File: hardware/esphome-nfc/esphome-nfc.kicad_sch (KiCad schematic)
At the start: 34 parts, among them U1 ESP32-C3-WROOM-02, U2 PN7160A1HN/C100Y, U3 AP2112K-3.3TRG1, U4 USBLC6-2P6, Y1 Crystal_GND24

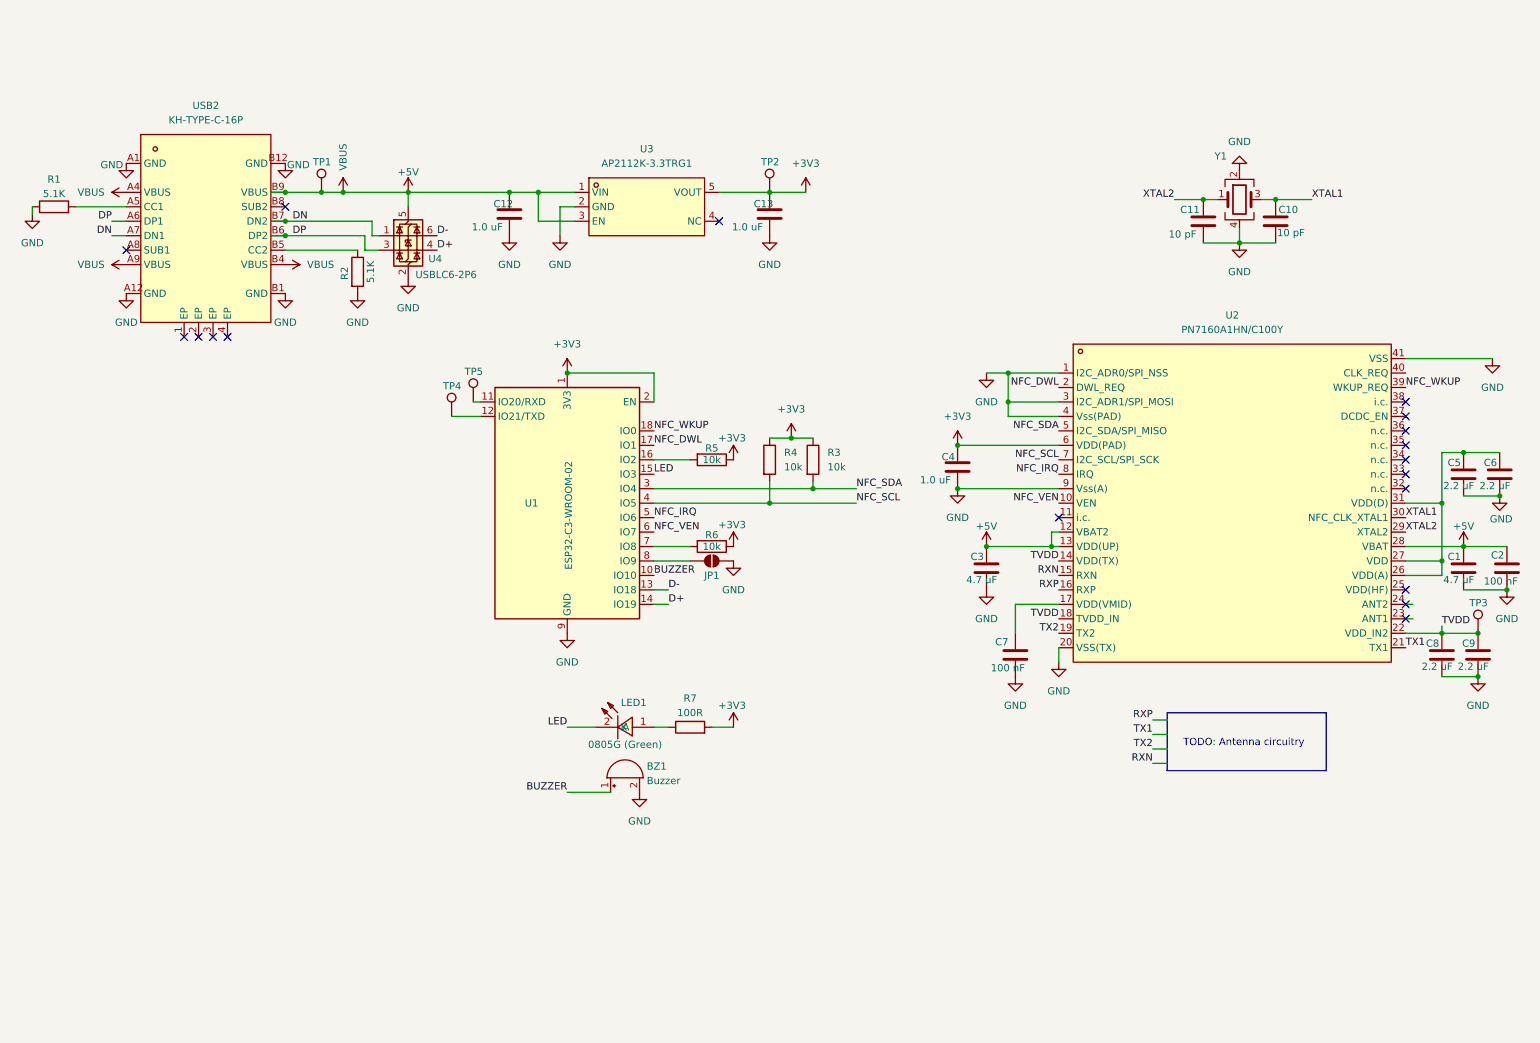
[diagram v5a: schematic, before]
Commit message: esphome-nfc final touches
* Add an antenna and corresponding matching circuitry
* Add a button (you never know...)
* Mark components I plan to solder manually as "Do Not Place"
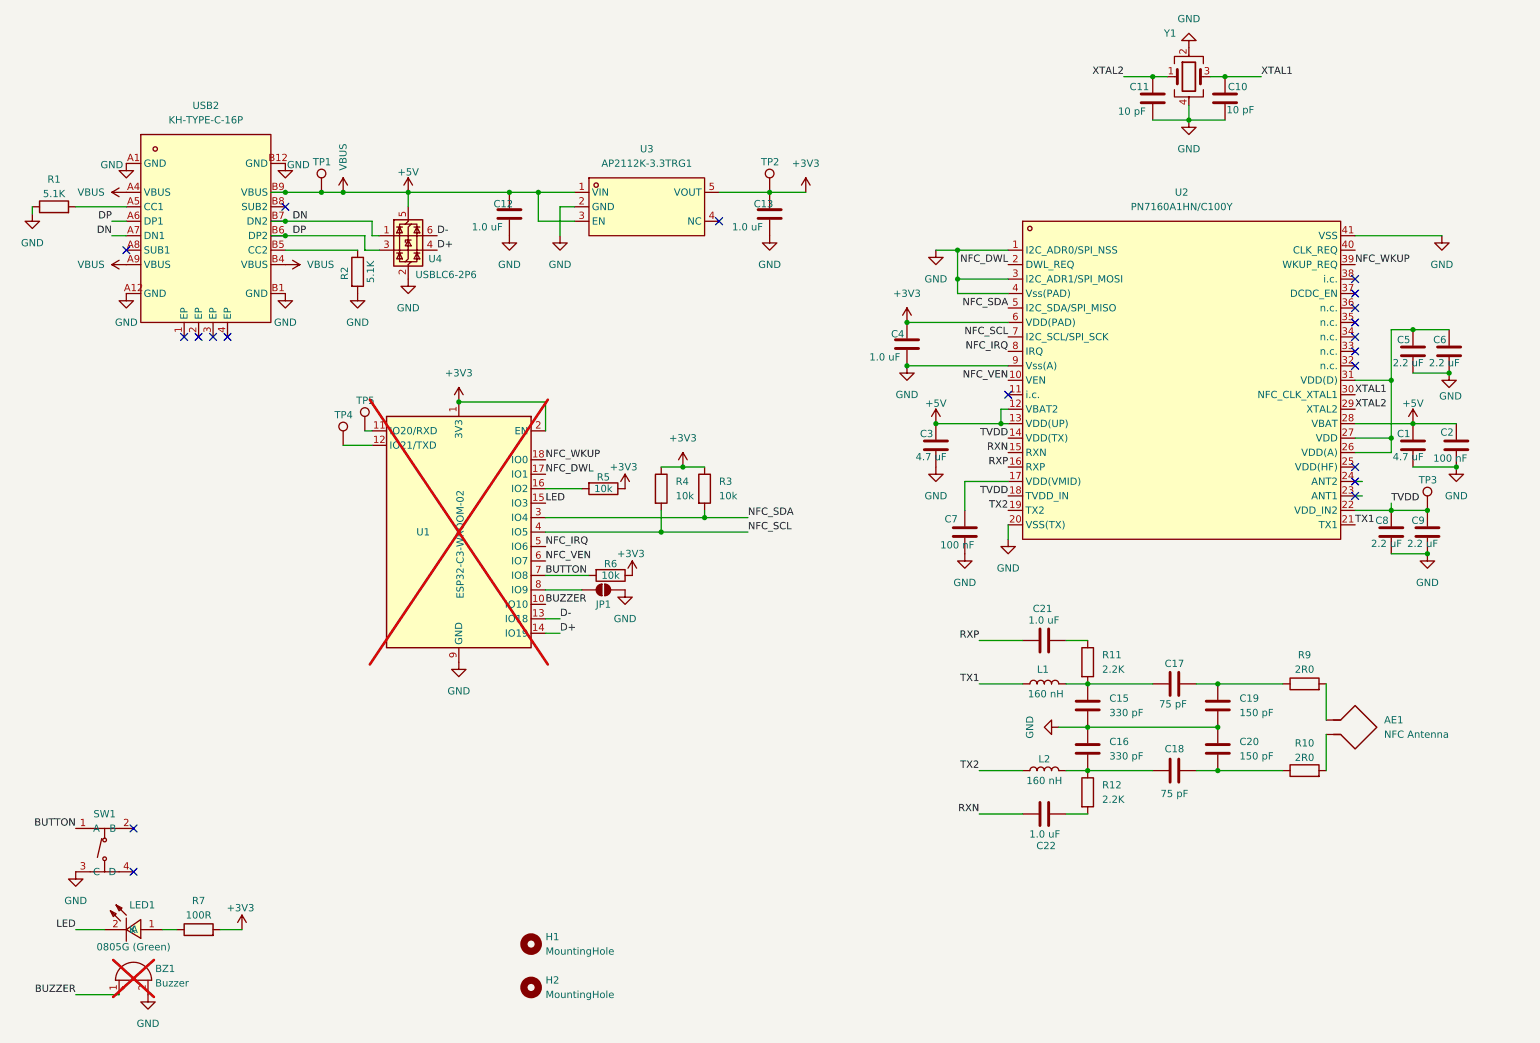
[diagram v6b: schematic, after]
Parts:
- added AE1: NFC Antenna, symbol Device:Antenna_Loop
- added C15, C16: 330 pF, Capacitor_SMD:C_0603_1608Metric, symbol Device:C
- added C17, C18: 75 pF, Capacitor_SMD:C_0402_1005Metric, symbol Device:C
- added C19, C20: 150 pF, Capacitor_SMD:C_0603_1608Metric, symbol Device:C
- added C21, C22: 1.0 uF, Capacitor_SMD:C_0603_1608Metric, symbol Ostranna:1.0 uF
- added H1, H2: MountingHole, MountingHole:MountingHole_2.7mm_M2.5, symbol Mechanical:MountingHole
- added L1, L2: 160 nH, Inductor_SMD:L_0603_1608Metric, symbol Device:L
- added R10, R9: 2R0, Resistor_SMD:R_1206_3216Metric, symbol Device:R
- added R11, R12: 2.2K, Resistor_SMD:R_0603_1608Metric, symbol Device:R
- added SW1: TS-1187A-B-A-B, easyeda2kicad:SW-SMD_4P-L5.1-W5.1-P3.70-LS6.5-TL-2, symbol easyeda2kicad:TS-1187A-B-A-B
- BZ1, U1: now not fitted
- C10, C11: footprint Capacitor_SMD:C_0402_1005Metric -> Capacitor_SMD:C_0603_1608Metric
- C5, C6, C8, C9: LCSC (none) -> C23630
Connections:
- net GND: now also C15.2, C16.1, C19.2, C20.1, SW1.3 (C)
- net RXN: now also C22.1
- net RXP: now also C21.2
- net TX1: now also L1.1
- net TX2: now also L2.1
- net BUTTON: now reaches R6.2, U1.7 (IO8)
- net BUTTON: now also SW1.1 (A)
- new net: C21.1, R11.1
- new net: C15.1, C17.1, L1.2, R11.2
- new net: C17.2, C19.1, R9.1
- new net: C16.2, C18.1, L2.2, R12.1
- new net: C18.2, C20.2, R10.1
- new net: C22.2, R12.2
- new net: AE1.1, R9.2
- new net: AE1.2, R10.2
- no-connect marks 18 -> 20
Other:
- note removed: "TODO: Antenna circuitry"
- moved on the sheet: C1, C10, C11, C2, C3, C4, C5, C6, C7, C8, C9, JP1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

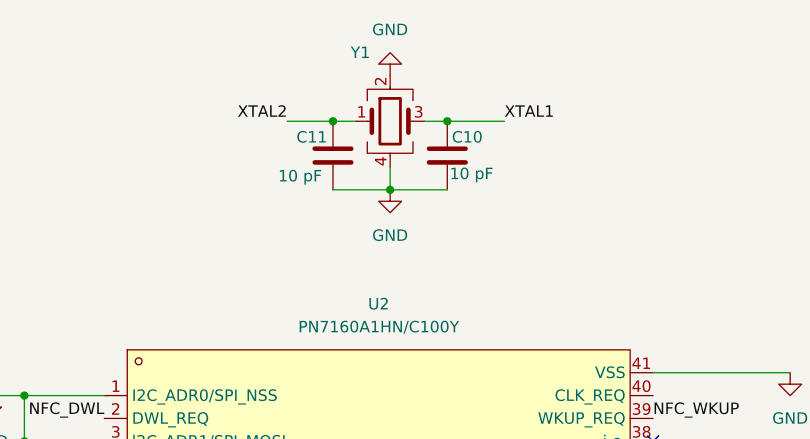
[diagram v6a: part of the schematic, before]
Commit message: Bump the capacitance of capacitors near the oscillator based on some reading
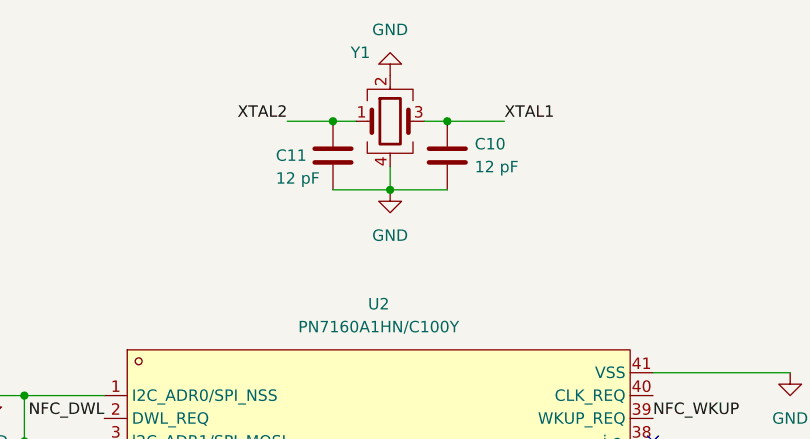
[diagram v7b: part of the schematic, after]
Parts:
- removed C10, C11: 10 pF, Capacitor_SMD:C_0603_1608Metric, symbol Ostranna:10 pF
- added C10, C11: 12 pF, Capacitor_SMD:C_0402_1005Metric, symbol Ostranna:12 pF
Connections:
- net GND: now also C10.2, C11.2
- net XTAL1: now also C10.1
- net XTAL2: now also C11.1
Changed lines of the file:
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@@
 	)
 	(junction
+		(at 231.14 25.4)
+		(diameter 0)
+		(color 0 0 0 0)
+	)
+	(junction
 		(at 132.08 105.41)
 		(diameter 0)
@@
 	)
 	(junction
-		(at 231.14 25.4)
-		(diameter 0)
-		(color 0 0 0 0)
-	)
-	(junction
 		(at 175.26 68.58)
 		(diameter 0)
@@
 	(wire
 		(pts
-			(xy 218.44 25.4) (xy 220.98 25.4)
+			(xy 213.36 25.4) (xy 218.44 25.4)
 		)
 		(stroke
@@
 	(wire
 		(pts
+			(xy 231.14 25.4) (xy 237.49 25.4)
+		)
+		(stroke
+			(width 0)
+			(type default)
+		)
+	)
+	(wire
+		(pts
 			(xy 254 101.6) (xy 260.35 101.6)
 		)
@@
 	(wire
 		(pts
+			(xy 218.44 25.4) (xy 220.98 25.4)
+		)
+		(stroke
+			(width 0)
+			(type default)
+		)
+	)
+	(wire
+		(pts
 			(xy 260.35 69.85) (xy 264.16 69.85)
 		)
@@
 	(wire
 		(pts
-			(xy 237.49 25.4) (xy 231.14 25.4)
-		)
-		(stroke
-			(width 0)
-			(type default)
-		)
-	)
-	(wire
-		(pts
 			(xy 191.77 86.36) (xy 193.04 86.36)
 		)
@@
 	(wire
 		(pts
-			(xy 213.36 25.4) (xy 218.44 25.4)
-		)
-		(stroke
-			(width 0)
-			(type default)
-		)
-	)
-	(wire
-		(pts
 			(xy 254 86.36) (xy 264.16 86.36)
 		)
@@
 	)
 	(symbol
-		(lib_id "Ostranna:10 pF")
-		(at 231.14 29.21 0)
-		(unit 1)
-		(exclude_from_sim no)
-		(in_bom yes)
-		(on_board yes)
-		(dnp no)
-		(property "Reference" "C10"
-			(at 231.648 27.178 0)
-			(effects
-				(font
-					(size 1.27 1.27)
-				)
-				(justify left)
-			)
-		)
-		(property "Value" "10 pF"
-			(at 231.394 31.242 0)
-			(effects
-				(font
-					(size 1.27 1.27)
-				)
-				(justify left)
-			)
-		)
-		(property "Footprint" "Capacitor_SMD:C_0603_1608Metric"
-			(at 234.188 34.544 0)
-			(effects
-				(font
-					(size 1.27 1.27)
-				)
-				(hide yes)
-			)
-		)
-		(property "Datasheet" "~"
-			(at 231.14 29.21 0)
-			(effects
-				(font
-					(size 1.27 1.27)
-				)
-				(hide yes)
-			)
-		)
-		(property "Description" "Capacitor to use near quartz crystals"
-			(at 231.14 28.956 0)
-			(effects
-				(font
-					(size 1.27 1.27)
-				)
-				(hide yes)
-			)
-		)
-		(property "LCSC" "C1634"
-			(at 237.744 25.908 0)
-			(effects
-				(font
-					(size 1.27 1.27)
-				)
-				(hide yes)
-			)
-		)
-		(property "LCSC type" "Basic"
-			(at 225.298 25.654 0)
-			(effects
-				(font
-					(size 1.27 1.27)
-				)
-				(hide yes)
-			)
-		)
-		(pin "1"
-		)
-		(pin "2"
-		)
-		(instances
-			(project ""
-				(path "/0388137f-fb41-46a6-bb35-a6e9549dd65e"
-					(reference "C10")
-					(unit 1)
-				)
-			)
-		)
-	)
-	(symbol
 		(lib_id "Connector:TestPoint")
 		(at 80.01 87.63 0)
@@
 	)
 	(symbol
+		(lib_id "Ostranna:12 pF")
+		(at 218.44 29.21 0)
+		(unit 1)
+		(exclude_from_sim no)
+		(in_bom yes)
+		(on_board yes)
+		(dnp no)
+		(property "Reference" "C11"
+			(at 212.09 29.21 0)
+			(effects
+				(font
+					(size 1.27 1.27)
+				)
+				(justify left)
+			)
+		)
+		(property "Value" "12 pF"
+			(at 212.09 31.75 0)
+			(effects
+				(font
+					(size 1.27 1.27)
+				)
+				(justify left)
+			)
+		)
+		(property "Footprint" "Capacitor_SMD:C_0402_1005Metric"
+			(at 220.98 35.052 0)
+			(effects
+				(font
+					(size 1.27 1.27)
+				)
+				(hide yes)
+			)
+		)
+		(property "Datasheet" "~"
+			(at 218.44 29.21 0)
+			(effects
+				(font
+					(size 1.27 1.27)
+				)
+				(hide yes)
+			)
+		)
+		(property "Description" "Capacitor to use near quartz crystals"
+			(at 220.218 24.892 0)
+			(effects
+				(font
+					(size 1.27 1.27)
+				)
+				(hide yes)
+			)
+		)
+		(property "LCSC" "C1547"
+			(at 226.06 28.956 0)
+			(effects
+				(font
+					(size 1.27 1.27)
+				)
+				(hide yes)
+			)
+		)
+		(property "LCSC type" "Basic"
+			(at 232.156 28.956 0)
+			(effects
+				(font
+					(size 1.27 1.27)
+				)
+				(hide yes)
+			)
+		)
+		(pin "2"
+		)
+		(pin "1"
+		)
+		(instances
+			(project ""
+				(path "/0388137f-fb41-46a6-bb35-a6e9549dd65e"
+					(reference "C11")
+					(unit 1)
+				)
+			)
+		)
+	)
+	(symbol
 		(lib_id "easyeda2kicad:PN7160A1HN_C100Y")
 		(at 223.52 78.74 0)
@@
 	)
 	(symbol
+		(lib_id "Ostranna:12 pF")
+		(at 231.14 29.21 0)
+		(unit 1)
+		(exclude_from_sim no)
+		(in_bom yes)
+		(on_board yes)
+		(dnp no)
+		(property "Reference" "C10"
+			(at 234.188 27.94 0)
+			(effects
+				(font
+					(size 1.27 1.27)
+				)
+				(justify left)
+			)
+		)
+		(property "Value" "12 pF"
+			(at 234.188 30.48 0)
+			(effects
+				(font
+					(size 1.27 1.27)
+				)
+				(justify left)
+			)
+		)
+		(property "Footprint" "Capacitor_SMD:C_0402_1005Metric"
+			(at 233.68 35.052 0)
+			(effects
+				(font
+					(size 1.27 1.27)
+				)
+				(hide yes)
+			)
+		)
+		(property "Datasheet" "~"
+			(at 231.14 29.21 0)
+			(effects
+				(font
+					(size 1.27 1.27)
+				)
+				(hide yes)
+			)
+		)
+		(property "Description" "Capacitor to use near quartz crystals"
+			(at 232.918 24.892 0)
+			(effects
+				(font
+					(size 1.27 1.27)
+				)
+				(hide yes)
+			)
+		)
+		(property "LCSC" "C1547"
+			(at 238.76 28.956 0)
+			(effects
+				(font
+					(size 1.27 1.27)
+				)
+				(hide yes)
+			)
+		)
+		(property "LCSC type" "Basic"
+			(at 244.856 28.956 0)
+			(effects
+				(font
+					(size 1.27 1.27)
+				)
+				(hide yes)
+			)
+		)
+		(pin "2"
+		)
+		(pin "1"
+		)
+		(instances
+			(project "esphome-nfc"
+				(path "/0388137f-fb41-46a6-bb35-a6e9549dd65e"
+					(reference "C10")
+					(unit 1)
+				)
+			)
+		)
+	)
+	(symbol
 		(lib_id "easyeda2kicad:AP2112K-3.3TRG1")
 		(at 129.54 48.26 0)
@@
 					(unit 1)
 				)
-			)
-		)
-	)
-	(symbol
-		(lib_id "Ostranna:10 pF")
-		(at 218.44 29.21 0)
-		(unit 1)
-		(exclude_from_sim no)
-		(in_bom yes)
-		(on_board yes)
-		(dnp no)
-		(property "Reference" "C11"
-			(at 214.376 27.178 0)
-			(effects
-				(font
-					(size 1.27 1.27)
-				)
-				(justify left)
-			)
-		)
-		(property "Value" "10 pF"
-			(at 212.344 31.496 0)
-			(effects
-				(font
-					(size 1.27 1.27)
-				)
-				(justify left)
-			)
-		)
-		(property "Footprint" "Capacitor_SMD:C_0603_1608Metric"
-			(at 221.488 34.544 0)
-			(effects
-				(font
-					(size 1.27 1.27)
-				)
-				(hide yes)
-			)
-		)
-		(property "Datasheet" "~"
-			(at 218.44 29.21 0)
-			(effects
-				(font
-					(size 1.27 1.27)
-				)
-				(hide yes)
-			)
-		)
-		(property "Description" "Capacitor to use near quartz crystals"
-			(at 218.44 28.956 0)
-			(effects
-				(font
-					(size 1.27 1.27)
-				)
-				(hide yes)
-			)
-		)
-		(property "LCSC" "C1634"
-			(at 225.044 25.908 0)
-			(effects
-				(font
-					(size 1.27 1.27)
-				)
-				(hide yes)
-			)
-		)
-		(property "LCSC type" "Basic"
-			(at 212.598 25.654 0)
-			(effects
-				(font
-					(size 1.27 1.27)
-				)
-				(hide yes)
-			)
-		)
-		(pin "1"
-		)
-		(pin "2"
-		)
-		(instances
-			(project "esphome-nfc"
-				(path "/0388137f-fb41-46a6-bb35-a6e9549dd65e"
-					(reference "C11")
-					(unit 1)
-				)

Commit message: Use easyeda blueprint for USBLC6-2P6 to fix the rotation
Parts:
- U4: footprint Package_TO_SOT_SMD:SOT-666 -> easyeda2kicad:SOT-666-6_L1.6-W1.2-P0.50-LS1.6-BR
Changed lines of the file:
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@@
 			)
 		)
-		(property "Footprint" "Package_TO_SOT_SMD:SOT-666"
+		(property "Footprint" "easyeda2kicad:SOT-666-6_L1.6-W1.2-P0.50-LS1.6-BR"
 			(at 88.646 60.071 0)
 			(effects
